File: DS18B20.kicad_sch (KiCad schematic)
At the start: 5 parts, among them J26 8P8C_Shielded, J27 8P8C_Shielded, J39 8P8C_Shielded, J40 8P8C_Shielded, J41 8P8C_Shielded

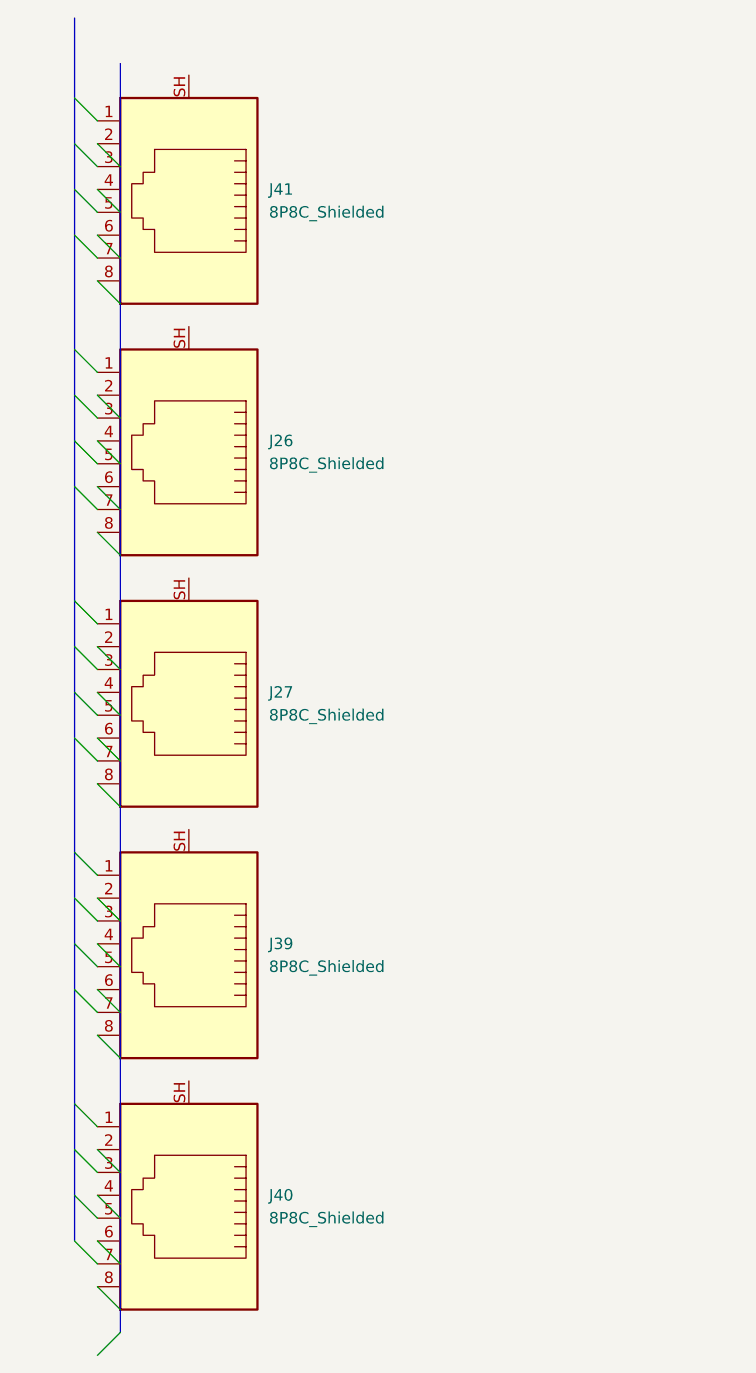
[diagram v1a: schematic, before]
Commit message: resistors for teams
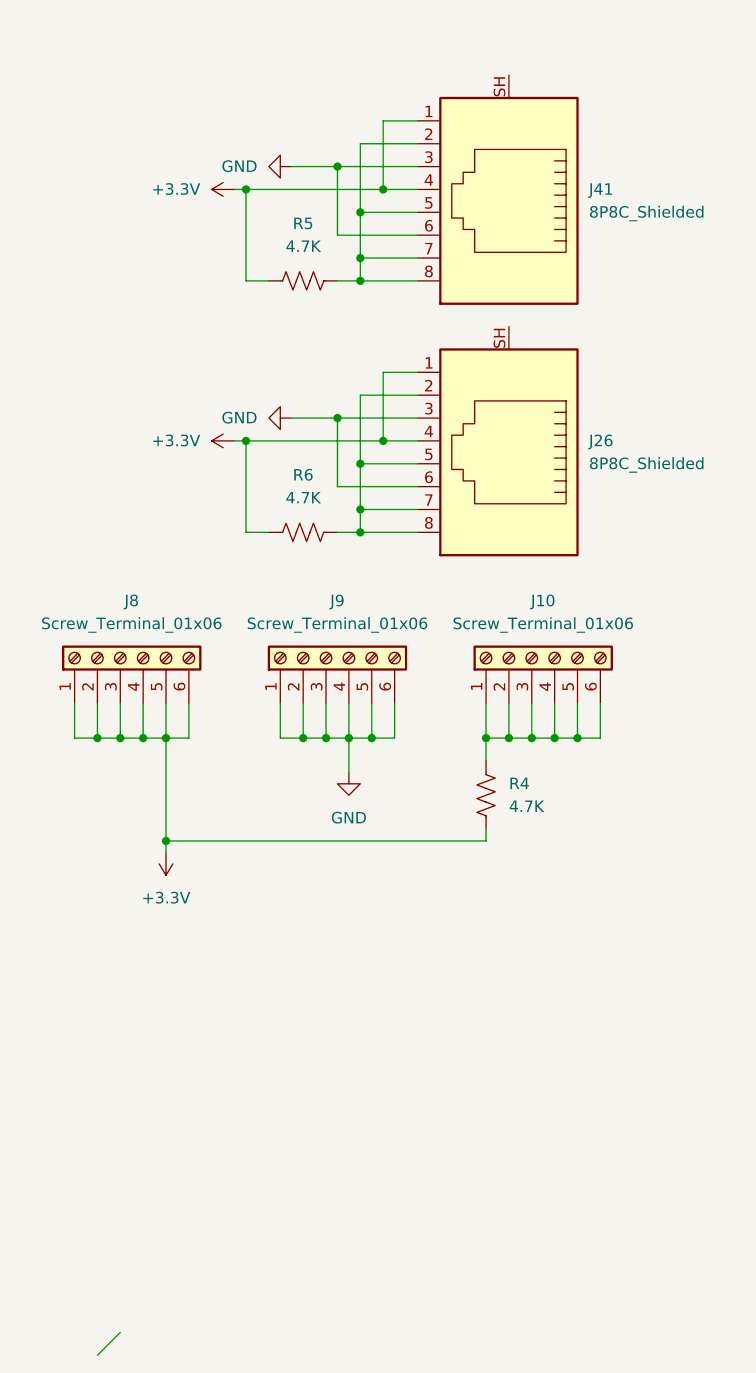
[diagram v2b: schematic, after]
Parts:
- removed J27, J39, J40: 8P8C_Shielded, Connector_RJ:RJ45_HALO_HFJ11-x2450HRL_Horizontal, symbol Connector:8P8C_Shielded
- added J10, J8, J9: Screw_Terminal_01x06, symbol Connector:Screw_Terminal_01x06
- added R4, R5, R6: 4.7K, symbol Device:R_US
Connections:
- net +3.3V: now reaches J41.1
- net +3.3V: now also J26.1, J26.4, J41.4, J8.1 (Pin_1), J8.2 (Pin_2), J8.3 (Pin_3), J8.4 (Pin_4), J8.5 (Pin_5), J8.6 (Pin_6), R4.2, R5.1, R6.1
- net at J41.2: now also J41.5, J41.7, J41.8, R5.2
- net GND: now reaches J41.3
- net GND: now also J26.3, J26.6, J41.6, J9.1 (Pin_1), J9.2 (Pin_2), J9.3 (Pin_3), J9.4 (Pin_4), J9.5 (Pin_5), J9.6 (Pin_6)
- net at J26.2: now also J26.5, J26.7, J26.8, R6.2
- new net: J10.1 (Pin_1), J10.2 (Pin_2), J10.3 (Pin_3), J10.4 (Pin_4), J10.5 (Pin_5), J10.6 (Pin_6), R4.1
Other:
- moved on the sheet: J26, J41

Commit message: slimmed down and spread out pcb
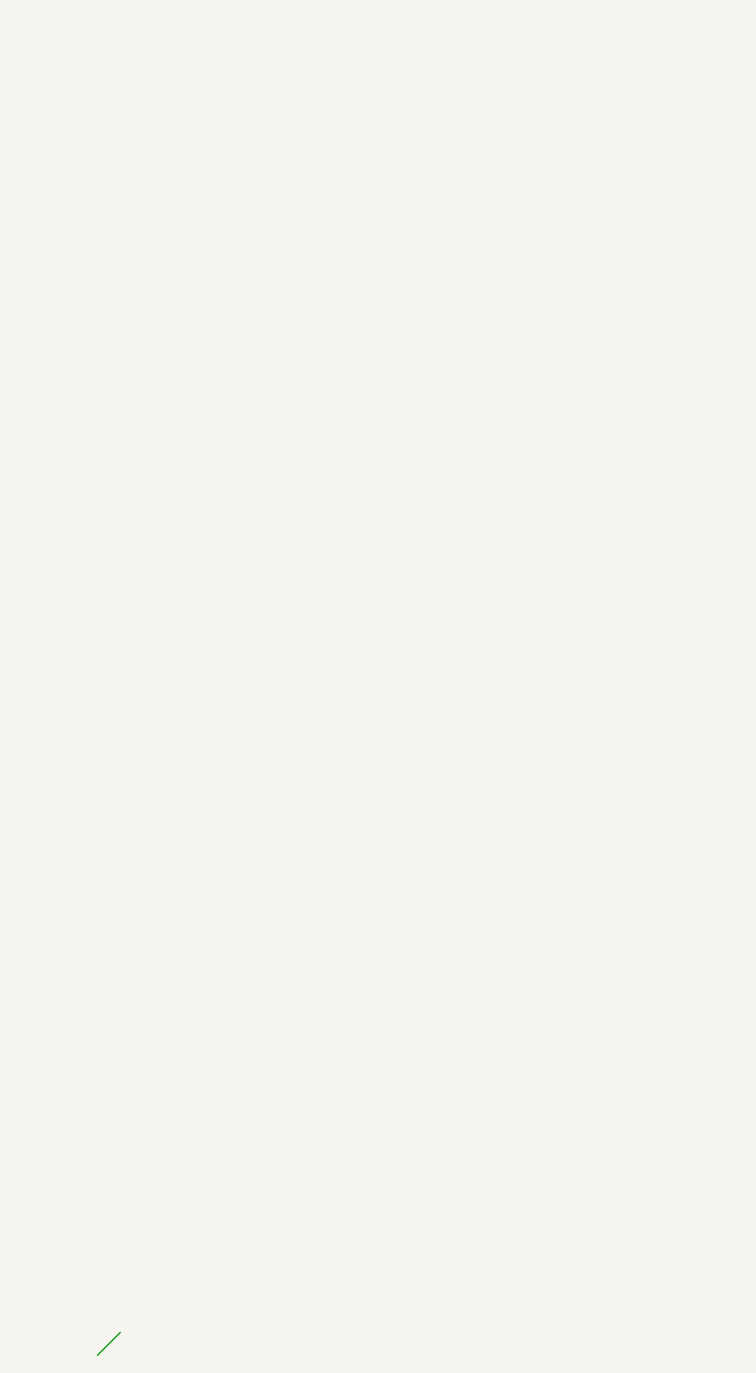
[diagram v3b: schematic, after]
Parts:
- removed J10, J8, J9: Screw_Terminal_01x06, symbol Connector:Screw_Terminal_01x06
- removed J26, J41: 8P8C_Shielded, Connector_RJ:RJ45_HALO_HFJ11-x2450HRL_Horizontal, symbol Connector:8P8C_Shielded
- removed R4, R5, R6: 4.7K, symbol Device:R_US
